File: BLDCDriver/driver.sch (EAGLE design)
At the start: 69 parts, among them Q1 NJM7800S, Q2 SIZ240DT-T1-GE3, Q3 SIZ240DT-T1-GE3, Q4 SIZ240DT-T1-GE3, U1 QFN50P400X400X100-25NDRV8300D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, U2 AS5048A-HTSP-500, U4 SOP80P620X125-8N

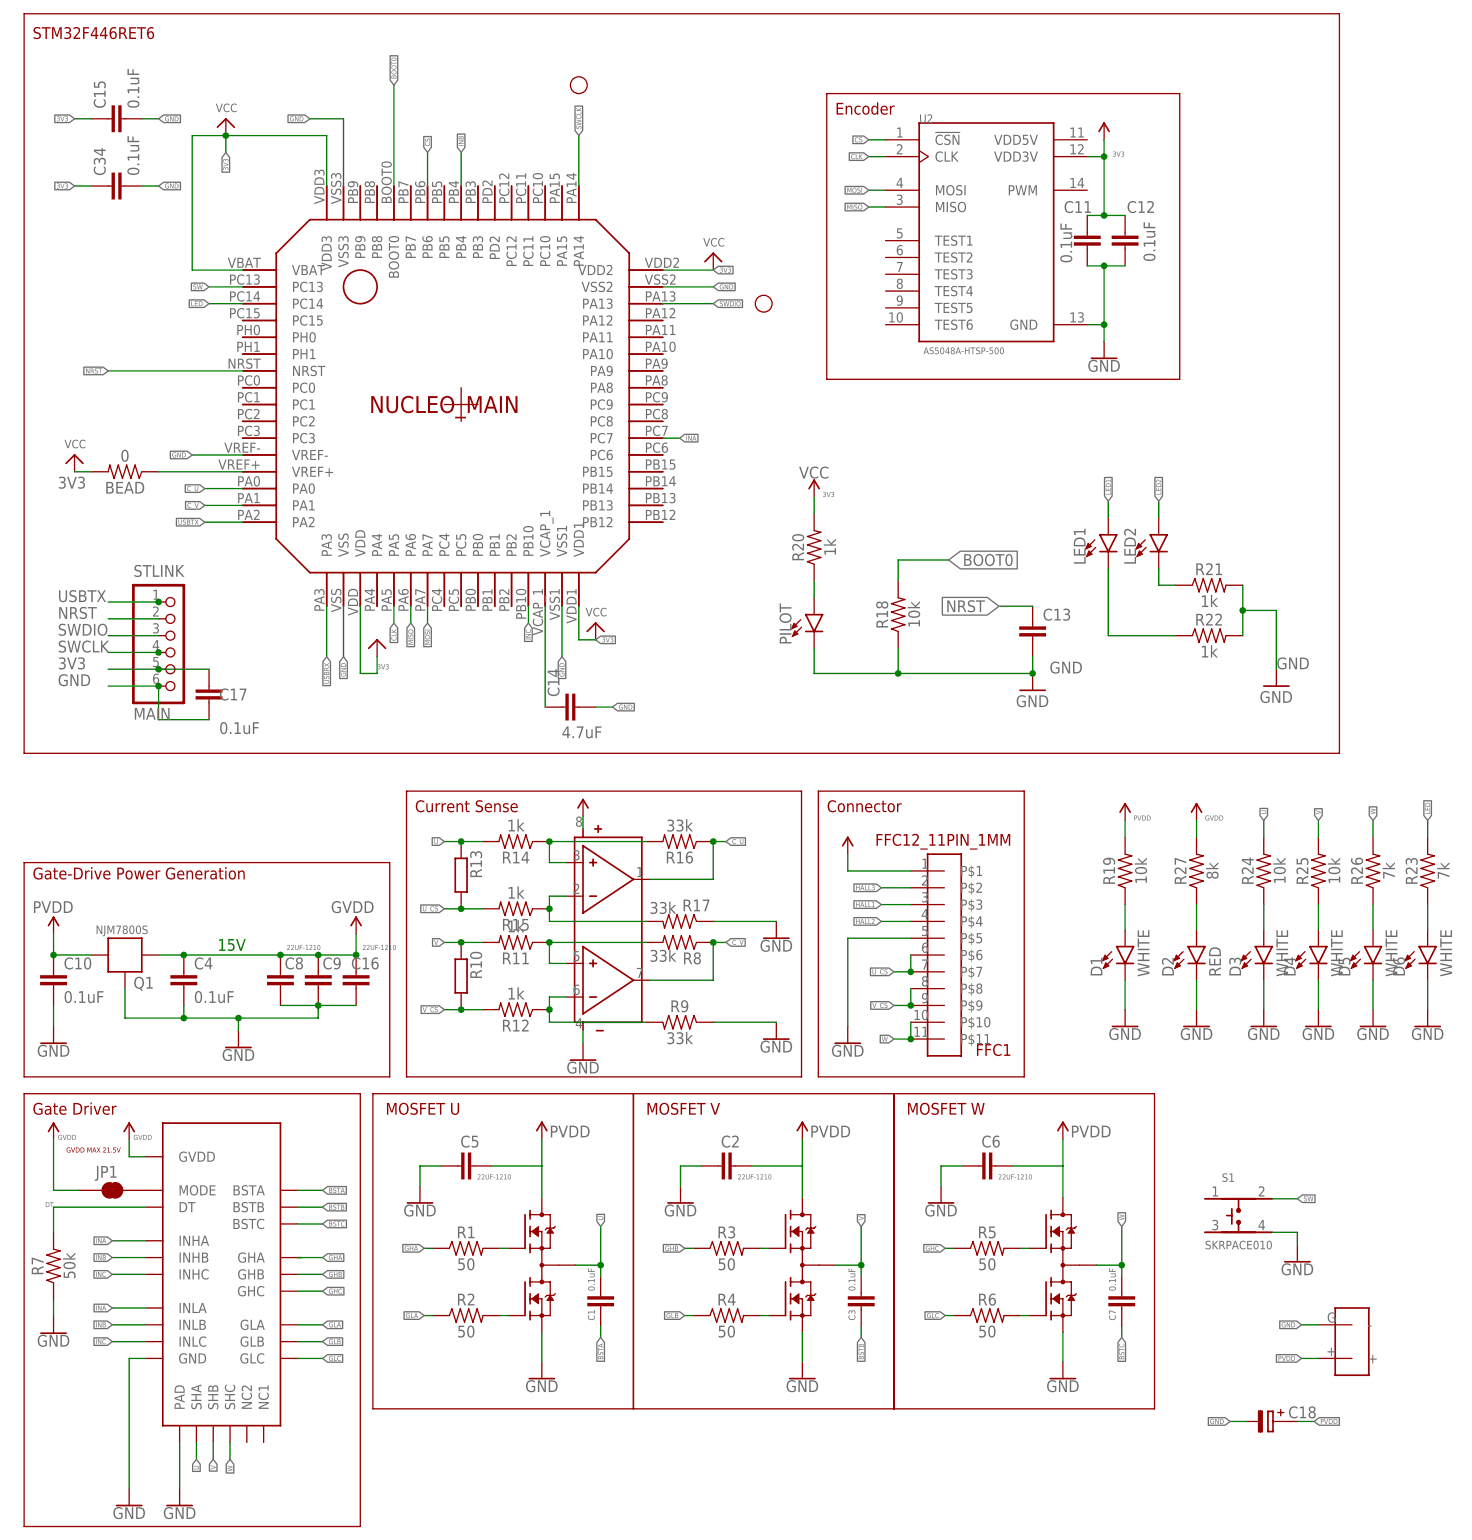
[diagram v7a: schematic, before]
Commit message: ちょっと頑張った
# ==== Emojis ====
# ✨ :sparkles: Add new feature
# ✅  :white_check_mark: Update existing feature (not bug)
# ⚠️  :warning: Fix bug/error
# 🔥  :fire: Remove files or features
# ✏️ :pencil2: Fix typos
# 📝  :memo: Update documentation
# ♻️  :recycle: Dependencies update
# 🐧  :penguin: Improved the Linux
# 🍎  :apple: Improved the macOS
# 🔖 :bookmark: Add new library
# 🎉  :tada: Initial commit

# ==== Format ====
# :emoji: Subject
#
# Commit body...

# ==== Messages ====
# 新規(ファイル)機能追加: Add
# 機能修正、既存機能追加（バグではない): Update
# リファクタリング: Clean
# ファイル名変更:
# 削除など: Remove
# バグ修正: Fix
# バージョンアップ: Upgrade
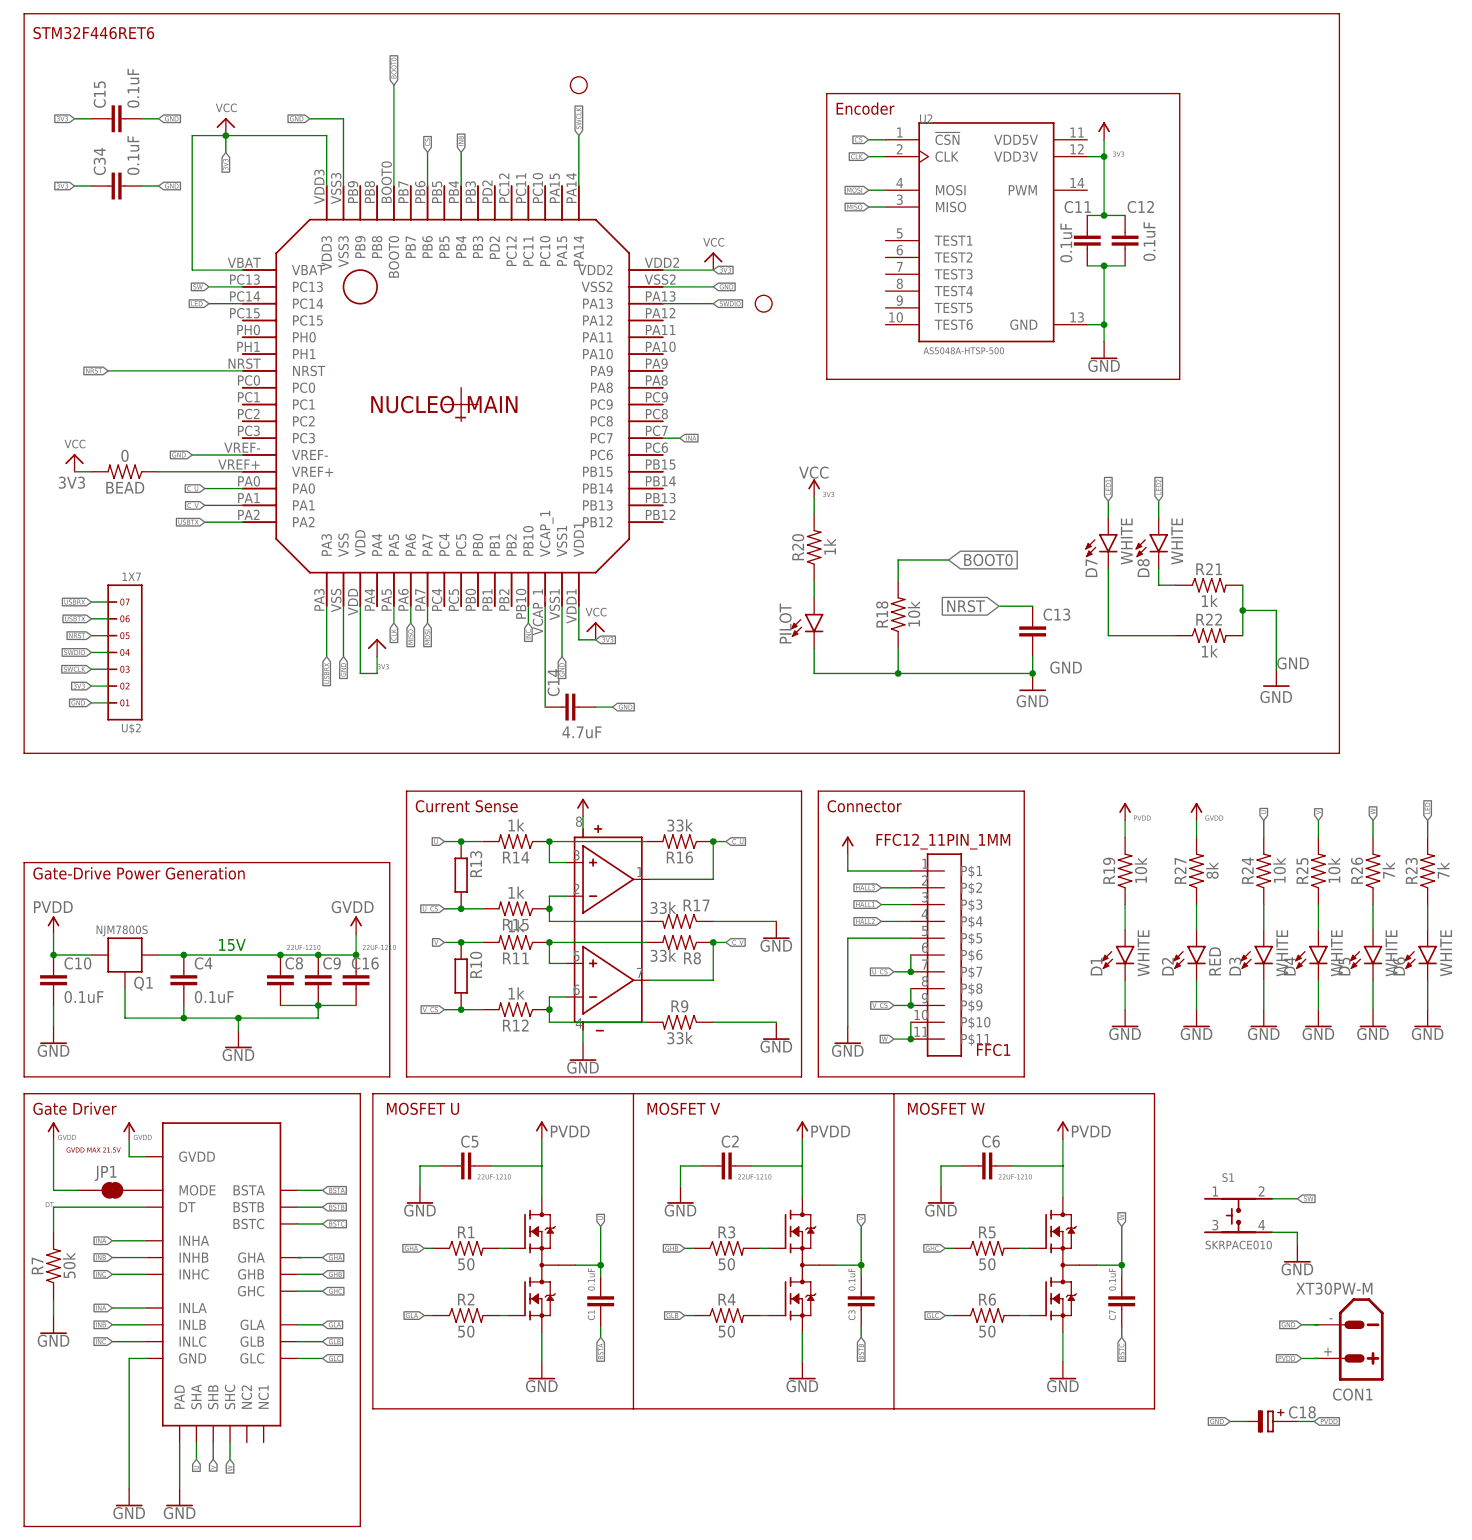
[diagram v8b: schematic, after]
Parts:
- removed C17: 0.1uF, Custom_Designed_By_Yusei:0.1UF_1608
- removed LED1, LED2: LED-SMD, Custom_Designed_By_Yusei:LED-SMD
- removed STLINK: MAIN, jst-xh:B6B-XH-A
- added CON1: XT30PW-M, XTn0 amass:XT30PW-M
- added D7, D8: WHITE, SparkFun-LED:LED-WHITE0603
- U$2: value BAT -> 1X7; device BAT:BAT -> headers(2mm):1X7
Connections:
- net N$1 renamed HB
- net N$2 renamed HA
- net N$4 renamed LA
- net N$5 renamed LB
- net N$6 renamed HC
- net N$7 renamed LC
- net 3V3: now also U$2.2; no longer C17.1, STLINK.5
- net GND: now also CON1.-, U$2.1; no longer C17.2, STLINK.6, U$2.-
- net LED1: now also D7.A; no longer LED1.A
- net LED2: now also D8.A; no longer LED2.A
- net N$12: now also D8.C; no longer LED2.C
- net N$13: now also D7.C; no longer LED1.C
- net NRST: now also U$2.5; no longer STLINK.2
- net PVDD: now also CON1.+; no longer U$2.+
- net SWCLK: now also U$2.3; no longer STLINK.4
- net SWDIO: now also U$2.4; no longer STLINK.3
- net USBRX: now also U$2.7
- net USBTX: now also U$2.6; no longer STLINK.1
